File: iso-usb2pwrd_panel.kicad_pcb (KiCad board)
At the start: 2 copper layers, 75 x 74 mm, 204 parts, among them J1 USB_C_Receptacle_USB2.0_14P, J2 USB_C_Receptacle_USB2.0_14P, U1 ADuM3165, U2 R05C1TF05S, U3 TPS25820, Y1 24Mhz

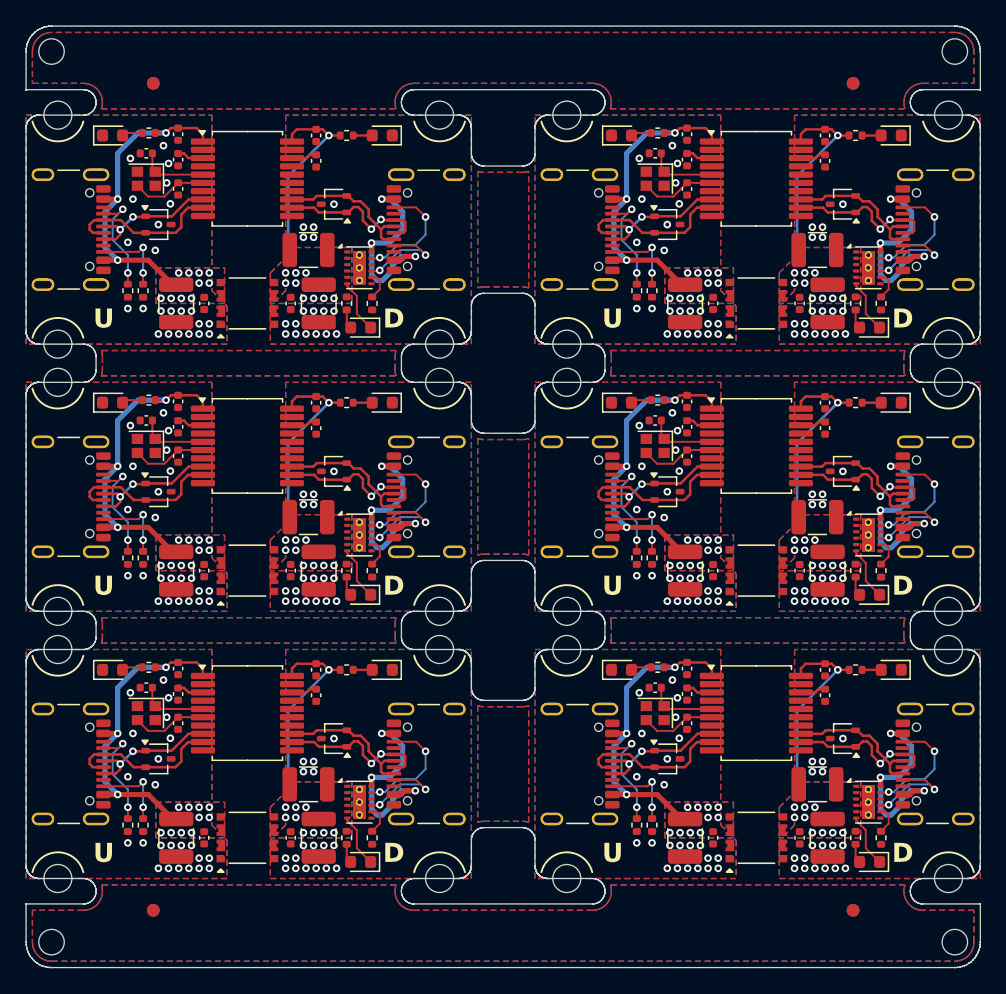
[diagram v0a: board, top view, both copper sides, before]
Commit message: update panel config: reduce vspace
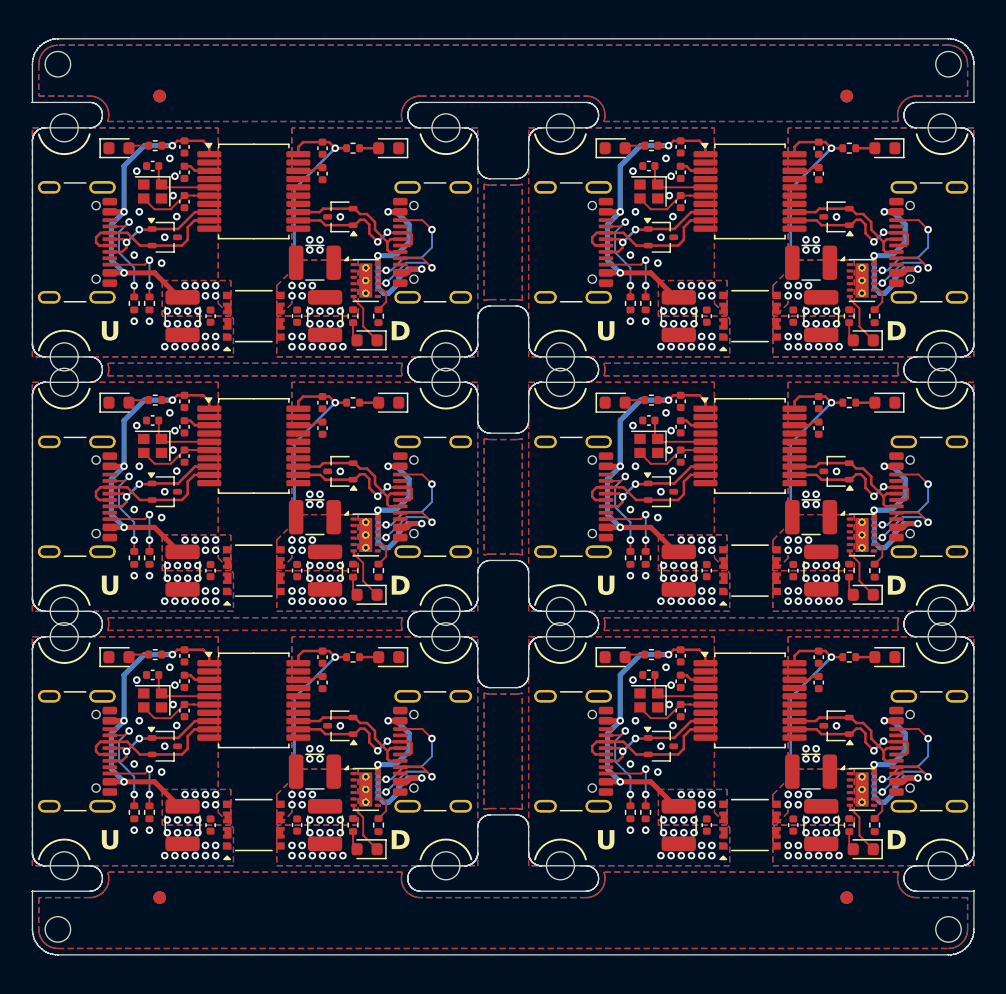
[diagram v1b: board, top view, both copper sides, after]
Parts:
- removed the C1 at (122.8, 84.8)
- removed the C1 at (122.8, 105.8)
- removed the C1 at (162.8, 126.8)
- removed the C1 at (162.8, 84.8)
- removed the C1 at (122.8, 126.8)
- removed the C1 at (162.8, 105.8)
- removed the C10 at (133.8, 71.6)
- removed the C10 at (173.8, 71.6)
- removed the C10 at (173.8, 92.6)
- removed the C10 at (133.8, 92.6)
- removed the C10 at (133.8, 113.6)
- removed the C10 at (173.8, 113.6)
- removed the C11 at (173.2, 122.6)
- removed the C11 at (133.2, 80.6)
- removed the C11 at (133.2, 122.6)
- removed the C11 at (173.2, 80.6)
- removed the C11 at (133.2, 101.6)
- removed the C11 at (173.2, 101.6)
- removed the C2 at (125.0, 84.8)
- removed the C2 at (125.0, 126.8)
- removed the C2 at (165.0, 84.8)
- removed the C2 at (125.0, 105.8)
- removed the C2 at (165.0, 126.8)
- removed the C2 at (165.0, 105.8)
- removed the C3 at (174.0, 84.8)
- removed the C3 at (134.0, 84.8)
- removed the C3 at (174.0, 105.8)
- removed the C3 at (174.0, 126.8)
- removed the C3 at (134.0, 126.8)
- removed the C3 at (134.0, 105.8)
- removed the C4 at (171.8, 84.8)
- removed the C4 at (131.8, 84.8)
- removed the C4 at (171.8, 105.8)
- removed the C4 at (171.8, 126.8)
- removed the C4 at (131.8, 126.8)
- removed the C4 at (131.8, 105.8)
- removed the C5 at (160.4, 94.0)
- removed the C5 at (160.4, 73.0)
- removed the C5 at (120.5, 94.0)
- removed the C5 at (120.5, 115.0)
- removed the C5 at (160.4, 115.0)
- removed the C5 at (120.5, 73.0)
- removed the C6 at (162.9, 75.8)
- removed the C6 at (162.9, 117.8)
- removed the C6 at (123.0, 117.8)
- removed the C6 at (123.0, 96.8)
- removed the C6 at (162.9, 96.8)
- removed the C6 at (123.0, 75.8)
- removed the C7 at (162.9, 94.5)
- removed the C7 at (123.0, 73.5)
- removed the C7 at (162.9, 115.5)
- removed the C7 at (123.0, 94.5)
- removed the C7 at (123.0, 115.5)
- removed the C7 at (162.9, 73.5)
- removed the C8 at (123.0, 92.5)
- removed the C8 at (162.9, 71.5)
- removed the C8 at (162.9, 113.5)
- removed the C8 at (162.9, 92.5)
- removed the C8 at (123.0, 71.5)
- removed the C8 at (123.0, 113.5)
- removed the C9 at (173.8, 73.6)
- removed the C9 at (173.8, 115.6)
- removed the C9 at (133.8, 73.6)
- removed the C9 at (133.8, 115.6)
- removed the C9 at (173.8, 94.6)
- removed the C9 at (133.8, 94.6)
- removed the D1 at (161.4, 78.6)
- removed the D1 at (161.4, 99.6)
- removed the D1 at (121.4, 78.6)
- removed the D1 at (121.4, 120.6)
- removed the D1 at (161.4, 120.6)
- removed the D1 at (121.4, 99.6)
- removed the D2 at (135.2, 119.0)
- removed the D2 at (135.2, 77.0)
- removed the D2 at (175.2, 98.0)
- removed the D2 at (175.2, 119.0)
- removed the D2 at (175.2, 77.0)
- removed the D2 at (135.2, 98.0)
- removed the D3 at (177.3, 128.7)
- removed the D3 at (137.3, 107.7)
- removed the D3 at (137.3, 128.7)
- removed the D3 at (177.3, 107.7)
- removed the D3 at (177.3, 86.7)
- removed the D3 at (137.3, 86.7)
- removed the D4 at (179.0, 92.6)
- removed the D4 at (139.0, 92.6)
- removed the D4 at (179.0, 113.6)
- removed the D4 at (139.0, 113.6)
- removed the D4 at (139.0, 71.6)
- removed the D4 at (179.0, 71.6)
- removed the D5 at (157.8, 113.6)
- removed the D5 at (157.8, 92.6)
- removed the D5 at (157.8, 71.6)
- removed the D5 at (117.8, 92.6)
- removed the D5 at (117.8, 113.6)
- removed the D5 at (117.8, 71.6)
- removed the H1 at (153.5, 109.0)
- removed the H1 at (153.5, 130.0)
- removed the H1 at (113.5, 88.0)
- removed the H1 at (153.5, 88.0)
- removed the H1 at (113.5, 109.0)
- removed the H1 at (113.5, 130.0)
- removed the H2 at (153.5, 91.0)
- removed the H2 at (113.5, 70.0)
- removed the H2 at (153.5, 112.0)
- removed the H2 at (113.5, 112.0)
- removed the H2 at (153.5, 70.0)
- removed the H2 at (113.5, 91.0)
- removed the H3 at (143.5, 112.0)
- removed the H3 at (183.5, 91.0)
- removed the H3 at (143.5, 70.0)
- removed the H3 at (183.5, 112.0)
- removed the H3 at (143.5, 91.0)
- removed the H3 at (183.5, 70.0)
- removed the H4 at (183.5, 88.0)
- removed the H4 at (143.5, 88.0)
- removed the H4 at (143.5, 109.0)
- removed the H4 at (183.5, 130.0)
- removed the H4 at (183.5, 109.0)
- removed the H4 at (143.5, 130.0)
- removed the J1 at (113.4, 79.0)
- removed the J1 at (113.4, 121.0)
- removed the J1 at (153.4, 121.0)
- removed the J1 at (113.4, 100.0)
- removed the J1 at (153.4, 100.0)
- removed the J1 at (153.4, 79.0)
- removed the J2 at (143.6, 121.0)
- removed the J2 at (183.6, 100.0)
- removed the J2 at (143.6, 79.0)
- removed the J2 at (143.6, 100.0)
- removed the J2 at (183.6, 121.0)
- removed the J2 at (183.6, 79.0)
- removed the R1 at (160.2, 83.8)
- removed the R1 at (120.2, 104.8)
- removed the R1 at (160.2, 104.8)
- removed the R1 at (120.2, 125.8)
- removed the R1 at (160.2, 125.8)
- removed the R1 at (120.2, 83.8)
- removed the R2 at (119.0, 104.8)
- removed the R2 at (159.0, 125.8)
- removed the R2 at (159.0, 104.8)
- removed the R2 at (119.0, 83.8)
- removed the R2 at (159.0, 83.8)
- removed the R2 at (119.0, 125.8)
- removed the R3 at (138.2, 126.8)
- removed the R3 at (178.2, 84.8)
- removed the R3 at (178.2, 126.8)
- removed the R3 at (138.2, 105.8)
- removed the R3 at (178.2, 105.8)
- removed the R3 at (138.2, 84.8)
- removed the R4 at (176.2, 84.8)
- removed the R4 at (136.2, 126.8)
- removed the R4 at (136.2, 84.8)
- removed the R4 at (176.2, 105.8)
- removed the R4 at (176.2, 126.8)
- removed the R4 at (136.2, 105.8)
- removed the R5 at (136.2, 113.6)
- removed the R5 at (136.2, 71.6)
- removed the R5 at (176.2, 113.6)
- removed the R5 at (176.2, 92.6)
- removed the R5 at (176.2, 71.6)
- removed the R5 at (136.2, 92.6)
- removed the R6 at (120.7, 113.4)
- removed the R6 at (160.7, 92.4)
- removed the R6 at (120.7, 71.4)
- removed the R6 at (160.7, 113.4)
- removed the R6 at (120.7, 92.4)
- removed the R6 at (160.7, 71.4)
- removed the U1 at (128.4, 75.0)
- removed the U1 at (128.4, 96.0)
- removed the U1 at (168.4, 96.0)
- removed the U1 at (168.4, 117.0)
- removed the U1 at (128.4, 117.0)
- removed the U1 at (168.4, 75.0)
- removed the U2 at (128.4, 84.8)
- removed the U2 at (128.4, 126.8)
- removed the U2 at (128.4, 105.8)
- removed the U2 at (168.4, 126.8)
- removed the U2 at (168.4, 84.8)
- removed the U2 at (168.4, 105.8)
- removed the U3 at (137.2, 82.0)
- removed the U3 at (137.2, 103.0)
- removed the U3 at (177.2, 103.0)
- removed the U3 at (137.2, 124.0)
- removed the U3 at (177.2, 82.0)
- removed the U3 at (177.2, 124.0)
- removed the Y1 at (160.4, 75.0)
- removed the Y1 at (160.4, 96.0)
- removed the Y1 at (120.5, 117.0)
- removed the Y1 at (120.5, 75.0)
- removed the Y1 at (120.5, 96.0)
- removed the Y1 at (160.4, 117.0)
- added C1: 22u, Capacitor_SMD:C_1210_3225Metric, F.Cu at (162.3, 85.8)
- added C1: 22u, Capacitor_SMD:C_1210_3225Metric, F.Cu at (162.3, 105.8)
- added C1: 22u, Capacitor_SMD:C_1210_3225Metric, F.Cu at (123.3, 105.8)
- added C1: 22u, Capacitor_SMD:C_1210_3225Metric, F.Cu at (123.3, 125.8)
- added C1: 22u, Capacitor_SMD:C_1210_3225Metric, F.Cu at (123.3, 85.8)
- added C1: 22u, Capacitor_SMD:C_1210_3225Metric, F.Cu at (162.3, 125.8)
- added C10: 0.1u, Capacitor_SMD:C_0402_1005Metric, F.Cu at (134.3, 112.6)
- added C10: 0.1u, Capacitor_SMD:C_0402_1005Metric, F.Cu at (173.3, 92.6)
- added C10: 0.1u, Capacitor_SMD:C_0402_1005Metric, F.Cu at (134.3, 92.6)
- added C10: 0.1u, Capacitor_SMD:C_0402_1005Metric, F.Cu at (173.3, 72.6)
- added C10: 0.1u, Capacitor_SMD:C_0402_1005Metric, F.Cu at (134.3, 72.6)
- added C10: 0.1u, Capacitor_SMD:C_0402_1005Metric, F.Cu at (173.3, 112.6)
- added C11: 22u, Capacitor_SMD:C_1210_3225Metric, F.Cu at (133.7, 81.6)
- added C11: 22u, Capacitor_SMD:C_1210_3225Metric, F.Cu at (172.7, 81.6)
- added C11: 22u, Capacitor_SMD:C_1210_3225Metric, F.Cu at (133.7, 121.6)
- added C11: 22u, Capacitor_SMD:C_1210_3225Metric, F.Cu at (172.7, 101.6)
- added C11: 22u, Capacitor_SMD:C_1210_3225Metric, F.Cu at (172.7, 121.6)
- added C11: 22u, Capacitor_SMD:C_1210_3225Metric, F.Cu at (133.7, 101.6)
- added C2: 0.1u, Capacitor_SMD:C_0402_1005Metric, F.Cu at (125.5, 105.8)
- added C2: 0.1u, Capacitor_SMD:C_0402_1005Metric, F.Cu at (164.5, 85.8)
- added C2: 0.1u, Capacitor_SMD:C_0402_1005Metric, F.Cu at (125.5, 85.8)
- added C2: 0.1u, Capacitor_SMD:C_0402_1005Metric, F.Cu at (164.5, 125.8)
- added C2: 0.1u, Capacitor_SMD:C_0402_1005Metric, F.Cu at (164.5, 105.8)
- added C2: 0.1u, Capacitor_SMD:C_0402_1005Metric, F.Cu at (125.5, 125.8)
- added C3: 22u, Capacitor_SMD:C_1210_3225Metric, F.Cu at (134.5, 125.8)
- added C3: 22u, Capacitor_SMD:C_1210_3225Metric, F.Cu at (173.5, 105.8)
- added C3: 22u, Capacitor_SMD:C_1210_3225Metric, F.Cu at (134.5, 85.8)
- added C3: 22u, Capacitor_SMD:C_1210_3225Metric, F.Cu at (134.5, 105.8)
- added C3: 22u, Capacitor_SMD:C_1210_3225Metric, F.Cu at (173.5, 125.8)
- added C3: 22u, Capacitor_SMD:C_1210_3225Metric, F.Cu at (173.5, 85.8)
- added C4: 0.1u, Capacitor_SMD:C_0402_1005Metric, F.Cu at (171.3, 105.8)
- added C4: 0.1u, Capacitor_SMD:C_0402_1005Metric, F.Cu at (132.3, 85.8)
- added C4: 0.1u, Capacitor_SMD:C_0402_1005Metric, F.Cu at (132.3, 125.8)
- added C4: 0.1u, Capacitor_SMD:C_0402_1005Metric, F.Cu at (171.3, 85.8)
- added C4: 0.1u, Capacitor_SMD:C_0402_1005Metric, F.Cu at (132.3, 105.8)
- added C4: 0.1u, Capacitor_SMD:C_0402_1005Metric, F.Cu at (171.3, 125.8)
- added C5: 15p, Capacitor_SMD:C_0402_1005Metric, F.Cu at (159.9, 94.0)
- added C5: 15p, Capacitor_SMD:C_0402_1005Metric, F.Cu at (159.9, 114.0)
- added C5: 15p, Capacitor_SMD:C_0402_1005Metric, F.Cu at (121.0, 114.0)
- added C5: 15p, Capacitor_SMD:C_0402_1005Metric, F.Cu at (121.0, 94.0)
- added C5: 15p, Capacitor_SMD:C_0402_1005Metric, F.Cu at (159.9, 74.0)
- added C5: 15p, Capacitor_SMD:C_0402_1005Metric, F.Cu at (121.0, 74.0)
- added C6: 15p, Capacitor_SMD:C_0402_1005Metric, F.Cu at (162.4, 96.8)
- added C6: 15p, Capacitor_SMD:C_0402_1005Metric, F.Cu at (123.5, 76.8)
- added C6: 15p, Capacitor_SMD:C_0402_1005Metric, F.Cu at (123.5, 96.8)
- added C6: 15p, Capacitor_SMD:C_0402_1005Metric, F.Cu at (123.5, 116.8)
- added C6: 15p, Capacitor_SMD:C_0402_1005Metric, F.Cu at (162.4, 76.8)
- added C6: 15p, Capacitor_SMD:C_0402_1005Metric, F.Cu at (162.4, 116.8)
- added C7: 0.1u, Capacitor_SMD:C_0402_1005Metric, F.Cu at (162.4, 114.5)
- added C7: 0.1u, Capacitor_SMD:C_0402_1005Metric, F.Cu at (162.4, 94.5)
- added C7: 0.1u, Capacitor_SMD:C_0402_1005Metric, F.Cu at (162.4, 74.5)
- added C7: 0.1u, Capacitor_SMD:C_0402_1005Metric, F.Cu at (123.5, 74.5)
- added C7: 0.1u, Capacitor_SMD:C_0402_1005Metric, F.Cu at (123.5, 94.5)
- added C7: 0.1u, Capacitor_SMD:C_0402_1005Metric, F.Cu at (123.5, 114.5)
- added C8: 0.1u, Capacitor_SMD:C_0402_1005Metric, F.Cu at (162.4, 92.5)
- added C8: 0.1u, Capacitor_SMD:C_0402_1005Metric, F.Cu at (123.5, 112.5)
- added C8: 0.1u, Capacitor_SMD:C_0402_1005Metric, F.Cu at (162.4, 112.5)
- added C8: 0.1u, Capacitor_SMD:C_0402_1005Metric, F.Cu at (123.5, 72.5)
- added C8: 0.1u, Capacitor_SMD:C_0402_1005Metric, F.Cu at (162.4, 72.5)
- added C8: 0.1u, Capacitor_SMD:C_0402_1005Metric, F.Cu at (123.5, 92.5)
- added C9: 0.1u, Capacitor_SMD:C_0402_1005Metric, F.Cu at (173.3, 114.6)
- added C9: 0.1u, Capacitor_SMD:C_0402_1005Metric, F.Cu at (173.3, 94.6)
- added C9: 0.1u, Capacitor_SMD:C_0402_1005Metric, F.Cu at (134.3, 74.6)
- added C9: 0.1u, Capacitor_SMD:C_0402_1005Metric, F.Cu at (134.3, 94.6)
- added C9: 0.1u, Capacitor_SMD:C_0402_1005Metric, F.Cu at (173.3, 74.6)
- added C9: 0.1u, Capacitor_SMD:C_0402_1005Metric, F.Cu at (134.3, 114.6)
- added D1: D_TVS_Dual_AAC, Package_TO_SOT_SMD:SOT-323_SC-70, F.Cu at (121.9, 79.6)
- added D1: D_TVS_Dual_AAC, Package_TO_SOT_SMD:SOT-323_SC-70, F.Cu at (160.9, 99.6)
- added D1: D_TVS_Dual_AAC, Package_TO_SOT_SMD:SOT-323_SC-70, F.Cu at (160.9, 119.6)
- added D1: D_TVS_Dual_AAC, Package_TO_SOT_SMD:SOT-323_SC-70, F.Cu at (121.9, 119.6)
- added D1: D_TVS_Dual_AAC, Package_TO_SOT_SMD:SOT-323_SC-70, F.Cu at (160.9, 79.6)
- added D1: D_TVS_Dual_AAC, Package_TO_SOT_SMD:SOT-323_SC-70, F.Cu at (121.9, 99.6)
- added D2: D_TVS_Dual_AAC, Package_TO_SOT_SMD:SOT-323_SC-70, F.Cu at (174.7, 118.0)
- added D2: D_TVS_Dual_AAC, Package_TO_SOT_SMD:SOT-323_SC-70, F.Cu at (174.7, 78.0)
- added D2: D_TVS_Dual_AAC, Package_TO_SOT_SMD:SOT-323_SC-70, F.Cu at (135.7, 78.0)
- added D2: D_TVS_Dual_AAC, Package_TO_SOT_SMD:SOT-323_SC-70, F.Cu at (174.7, 98.0)
- added D2: D_TVS_Dual_AAC, Package_TO_SOT_SMD:SOT-323_SC-70, F.Cu at (135.7, 118.0)
- added D2: D_TVS_Dual_AAC, Package_TO_SOT_SMD:SOT-323_SC-70, F.Cu at (135.7, 98.0)
- added D3: LED_Amber, LED_SMD:LED_0603_1608Metric, F.Cu at (137.8, 127.7)
- added D3: LED_Amber, LED_SMD:LED_0603_1608Metric, F.Cu at (176.8, 87.7)
- added D3: LED_Amber, LED_SMD:LED_0603_1608Metric, F.Cu at (176.8, 127.7)
- added D3: LED_Amber, LED_SMD:LED_0603_1608Metric, F.Cu at (137.8, 87.7)
- added D3: LED_Amber, LED_SMD:LED_0603_1608Metric, F.Cu at (176.8, 107.7)
- added D3: LED_Amber, LED_SMD:LED_0603_1608Metric, F.Cu at (137.8, 107.7)
- added D4: LED_Green, LED_SMD:LED_0603_1608Metric, F.Cu at (139.5, 92.6)
- added D4: LED_Green, LED_SMD:LED_0603_1608Metric, F.Cu at (178.5, 72.6)
- added D4: LED_Green, LED_SMD:LED_0603_1608Metric, F.Cu at (178.5, 92.6)
- added D4: LED_Green, LED_SMD:LED_0603_1608Metric, F.Cu at (178.5, 112.6)
- added D4: LED_Green, LED_SMD:LED_0603_1608Metric, F.Cu at (139.5, 72.6)
- added D4: LED_Green, LED_SMD:LED_0603_1608Metric, F.Cu at (139.5, 112.6)
- added D5: LED_Green, LED_SMD:LED_0603_1608Metric, F.Cu at (118.3, 72.6)
- added D5: LED_Green, LED_SMD:LED_0603_1608Metric, F.Cu at (118.3, 112.6)
- added D5: LED_Green, LED_SMD:LED_0603_1608Metric, F.Cu at (157.3, 112.6)
- added D5: LED_Green, LED_SMD:LED_0603_1608Metric, F.Cu at (157.3, 72.6)
- added D5: LED_Green, LED_SMD:LED_0603_1608Metric, F.Cu at (118.3, 92.6)
- added D5: LED_Green, LED_SMD:LED_0603_1608Metric, F.Cu at (157.3, 92.6)
- added H1: MountingHole, MountingHole:MountingHole_2.2mm_M2, F.Cu at (114.0, 109.0)
- added H1: MountingHole, MountingHole:MountingHole_2.2mm_M2, F.Cu at (153.0, 109.0)
- added H1: MountingHole, MountingHole:MountingHole_2.2mm_M2, F.Cu at (114.0, 129.0)
- added H1: MountingHole, MountingHole:MountingHole_2.2mm_M2, F.Cu at (153.0, 129.0)
- added H1: MountingHole, MountingHole:MountingHole_2.2mm_M2, F.Cu at (153.0, 89.0)
- added H1: MountingHole, MountingHole:MountingHole_2.2mm_M2, F.Cu at (114.0, 89.0)
- added H2: MountingHole, MountingHole:MountingHole_2.2mm_M2, F.Cu at (153.0, 111.0)
- added H2: MountingHole, MountingHole:MountingHole_2.2mm_M2, F.Cu at (114.0, 111.0)
- added H2: MountingHole, MountingHole:MountingHole_2.2mm_M2, F.Cu at (153.0, 71.0)
- added H2: MountingHole, MountingHole:MountingHole_2.2mm_M2, F.Cu at (114.0, 91.0)
- added H2: MountingHole, MountingHole:MountingHole_2.2mm_M2, F.Cu at (114.0, 71.0)
- added H2: MountingHole, MountingHole:MountingHole_2.2mm_M2, F.Cu at (153.0, 91.0)
- added H3: MountingHole, MountingHole:MountingHole_2.2mm_M2, F.Cu at (183.0, 71.0)
- added H3: MountingHole, MountingHole:MountingHole_2.2mm_M2, F.Cu at (144.0, 111.0)
- added H3: MountingHole, MountingHole:MountingHole_2.2mm_M2, F.Cu at (144.0, 91.0)
- added H3: MountingHole, MountingHole:MountingHole_2.2mm_M2, F.Cu at (183.0, 91.0)
- added H3: MountingHole, MountingHole:MountingHole_2.2mm_M2, F.Cu at (144.0, 71.0)
- added H3: MountingHole, MountingHole:MountingHole_2.2mm_M2, F.Cu at (183.0, 111.0)
- added H4: MountingHole, MountingHole:MountingHole_2.2mm_M2, F.Cu at (183.0, 109.0)
- added H4: MountingHole, MountingHole:MountingHole_2.2mm_M2, F.Cu at (144.0, 89.0)
- added H4: MountingHole, MountingHole:MountingHole_2.2mm_M2, F.Cu at (144.0, 109.0)
- added H4: MountingHole, MountingHole:MountingHole_2.2mm_M2, F.Cu at (183.0, 129.0)
- added H4: MountingHole, MountingHole:MountingHole_2.2mm_M2, F.Cu at (144.0, 129.0)
- added H4: MountingHole, MountingHole:MountingHole_2.2mm_M2, F.Cu at (183.0, 89.0)
- added J1: USB_C_Receptacle_USB2.0_14P, Connector_USB:USB_C_Receptacle_GCT_USB4105-xx-A_16P_TopMnt_Horizontal, F.Cu at (152.9, 120.0)
- added J1: USB_C_Receptacle_USB2.0_14P, Connector_USB:USB_C_Receptacle_GCT_USB4105-xx-A_16P_TopMnt_Horizontal, F.Cu at (113.9, 80.0)
- added J1: USB_C_Receptacle_USB2.0_14P, Connector_USB:USB_C_Receptacle_GCT_USB4105-xx-A_16P_TopMnt_Horizontal, F.Cu at (152.9, 80.0)
- added J1: USB_C_Receptacle_USB2.0_14P, Connector_USB:USB_C_Receptacle_GCT_USB4105-xx-A_16P_TopMnt_Horizontal, F.Cu at (113.9, 120.0)
- added J1: USB_C_Receptacle_USB2.0_14P, Connector_USB:USB_C_Receptacle_GCT_USB4105-xx-A_16P_TopMnt_Horizontal, F.Cu at (152.9, 100.0)
- added J1: USB_C_Receptacle_USB2.0_14P, Connector_USB:USB_C_Receptacle_GCT_USB4105-xx-A_16P_TopMnt_Horizontal, F.Cu at (113.9, 100.0)
- added J2: USB_C_Receptacle_USB2.0_14P, Connector_USB:USB_C_Receptacle_GCT_USB4105-xx-A_16P_TopMnt_Horizontal, F.Cu at (144.1, 100.0)
- added J2: USB_C_Receptacle_USB2.0_14P, Connector_USB:USB_C_Receptacle_GCT_USB4105-xx-A_16P_TopMnt_Horizontal, F.Cu at (144.1, 80.0)
- added J2: USB_C_Receptacle_USB2.0_14P, Connector_USB:USB_C_Receptacle_GCT_USB4105-xx-A_16P_TopMnt_Horizontal, F.Cu at (183.1, 120.0)
- added J2: USB_C_Receptacle_USB2.0_14P, Connector_USB:USB_C_Receptacle_GCT_USB4105-xx-A_16P_TopMnt_Horizontal, F.Cu at (144.1, 120.0)
- added J2: USB_C_Receptacle_USB2.0_14P, Connector_USB:USB_C_Receptacle_GCT_USB4105-xx-A_16P_TopMnt_Horizontal, F.Cu at (183.1, 80.0)
- added J2: USB_C_Receptacle_USB2.0_14P, Connector_USB:USB_C_Receptacle_GCT_USB4105-xx-A_16P_TopMnt_Horizontal, F.Cu at (183.1, 100.0)
- added R1: 5.1K, Resistor_SMD:R_0402_1005Metric, F.Cu at (159.7, 104.8)
- added R1: 5.1K, Resistor_SMD:R_0402_1005Metric, F.Cu at (120.7, 84.8)
- added R1: 5.1K, Resistor_SMD:R_0402_1005Metric, F.Cu at (120.7, 124.8)
- added R1: 5.1K, Resistor_SMD:R_0402_1005Metric, F.Cu at (159.7, 124.8)
- added R1: 5.1K, Resistor_SMD:R_0402_1005Metric, F.Cu at (159.7, 84.8)
- added R1: 5.1K, Resistor_SMD:R_0402_1005Metric, F.Cu at (120.7, 104.8)
- added R2: 5.1K, Resistor_SMD:R_0402_1005Metric, F.Cu at (158.5, 84.8)
- added R2: 5.1K, Resistor_SMD:R_0402_1005Metric, F.Cu at (119.5, 124.8)
- added R2: 5.1K, Resistor_SMD:R_0402_1005Metric, F.Cu at (119.5, 84.8)
- added R2: 5.1K, Resistor_SMD:R_0402_1005Metric, F.Cu at (158.5, 124.8)
- added R2: 5.1K, Resistor_SMD:R_0402_1005Metric, F.Cu at (158.5, 104.8)
- added R2: 5.1K, Resistor_SMD:R_0402_1005Metric, F.Cu at (119.5, 104.8)
- added R3: 100K, Resistor_SMD:R_0402_1005Metric, F.Cu at (138.7, 85.8)
- added R3: 100K, Resistor_SMD:R_0402_1005Metric, F.Cu at (138.7, 125.8)
- added R3: 100K, Resistor_SMD:R_0402_1005Metric, F.Cu at (177.7, 105.8)
- added R3: 100K, Resistor_SMD:R_0402_1005Metric, F.Cu at (177.7, 85.8)
- added R3: 100K, Resistor_SMD:R_0402_1005Metric, F.Cu at (138.7, 105.8)
- added R3: 100K, Resistor_SMD:R_0402_1005Metric, F.Cu at (177.7, 125.8)
- added R4: 5.1K, Resistor_SMD:R_0402_1005Metric, F.Cu at (175.7, 105.8)
- added R4: 5.1K, Resistor_SMD:R_0402_1005Metric, F.Cu at (136.7, 85.8)
- added R4: 5.1K, Resistor_SMD:R_0402_1005Metric, F.Cu at (136.7, 105.8)
- added R4: 5.1K, Resistor_SMD:R_0402_1005Metric, F.Cu at (136.7, 125.8)
- added R4: 5.1K, Resistor_SMD:R_0402_1005Metric, F.Cu at (175.7, 125.8)
- added R4: 5.1K, Resistor_SMD:R_0402_1005Metric, F.Cu at (175.7, 85.8)
- added R5: 5.1K, Resistor_SMD:R_0402_1005Metric, F.Cu at (136.7, 112.6)
- added R5: 5.1K, Resistor_SMD:R_0402_1005Metric, F.Cu at (175.7, 112.6)
- added R5: 5.1K, Resistor_SMD:R_0402_1005Metric, F.Cu at (136.7, 92.6)
- added R5: 5.1K, Resistor_SMD:R_0402_1005Metric, F.Cu at (175.7, 72.6)
- added R5: 5.1K, Resistor_SMD:R_0402_1005Metric, F.Cu at (136.7, 72.6)
- added R5: 5.1K, Resistor_SMD:R_0402_1005Metric, F.Cu at (175.7, 92.6)
- added R6: 5.1K, Resistor_SMD:R_0402_1005Metric, F.Cu at (121.2, 92.4)
- added R6: 5.1K, Resistor_SMD:R_0402_1005Metric, F.Cu at (160.2, 112.4)
- added R6: 5.1K, Resistor_SMD:R_0402_1005Metric, F.Cu at (160.2, 72.4)
- added R6: 5.1K, Resistor_SMD:R_0402_1005Metric, F.Cu at (160.2, 92.4)
- added R6: 5.1K, Resistor_SMD:R_0402_1005Metric, F.Cu at (121.2, 112.4)
- added R6: 5.1K, Resistor_SMD:R_0402_1005Metric, F.Cu at (121.2, 72.4)
- added U1: ADuM3165, Package_SO:SSOP-20_5.3x7.2mm_P0.65mm, F.Cu at (128.9, 96.0)
- added U1: ADuM3165, Package_SO:SSOP-20_5.3x7.2mm_P0.65mm, F.Cu at (167.9, 96.0)
- added U1: ADuM3165, Package_SO:SSOP-20_5.3x7.2mm_P0.65mm, F.Cu at (167.9, 76.0)
- added U1: ADuM3165, Package_SO:SSOP-20_5.3x7.2mm_P0.65mm, F.Cu at (167.9, 116.0)
- added U1: ADuM3165, Package_SO:SSOP-20_5.3x7.2mm_P0.65mm, F.Cu at (128.9, 76.0)
- added U1: ADuM3165, Package_SO:SSOP-20_5.3x7.2mm_P0.65mm, F.Cu at (128.9, 116.0)
- added U2: R05C1TF05S, q-lab:Package_LGA-12_5x4mm, F.Cu at (128.9, 105.8)
- added U2: R05C1TF05S, q-lab:Package_LGA-12_5x4mm, F.Cu at (128.9, 85.8)
- added U2: R05C1TF05S, q-lab:Package_LGA-12_5x4mm, F.Cu at (167.9, 85.8)
- added U2: R05C1TF05S, q-lab:Package_LGA-12_5x4mm, F.Cu at (128.9, 125.8)
- added U2: R05C1TF05S, q-lab:Package_LGA-12_5x4mm, F.Cu at (167.9, 105.8)
- added U2: R05C1TF05S, q-lab:Package_LGA-12_5x4mm, F.Cu at (167.9, 125.8)
- added U3: TPS25820, Package_SON:WSON-12-1EP_3x2mm_P0.5mm_EP1x2.65_ThermalVias, F.Cu at (176.7, 83.0)
- added U3: TPS25820, Package_SON:WSON-12-1EP_3x2mm_P0.5mm_EP1x2.65_ThermalVias, F.Cu at (176.7, 123.0)
- added U3: TPS25820, Package_SON:WSON-12-1EP_3x2mm_P0.5mm_EP1x2.65_ThermalVias, F.Cu at (137.7, 103.0)
- added U3: TPS25820, Package_SON:WSON-12-1EP_3x2mm_P0.5mm_EP1x2.65_ThermalVias, F.Cu at (137.7, 123.0)
- added U3: TPS25820, Package_SON:WSON-12-1EP_3x2mm_P0.5mm_EP1x2.65_ThermalVias, F.Cu at (176.7, 103.0)
- added U3: TPS25820, Package_SON:WSON-12-1EP_3x2mm_P0.5mm_EP1x2.65_ThermalVias, F.Cu at (137.7, 83.0)
- added Y1: 24Mhz, Crystal:Crystal_SMD_2016-4Pin_2.0x1.6mm, F.Cu at (159.9, 96.0)
- added Y1: 24Mhz, Crystal:Crystal_SMD_2016-4Pin_2.0x1.6mm, F.Cu at (159.9, 76.0)
- added Y1: 24Mhz, Crystal:Crystal_SMD_2016-4Pin_2.0x1.6mm, F.Cu at (121.0, 96.0)
- added Y1: 24Mhz, Crystal:Crystal_SMD_2016-4Pin_2.0x1.6mm, F.Cu at (121.0, 76.0)
- added Y1: 24Mhz, Crystal:Crystal_SMD_2016-4Pin_2.0x1.6mm, F.Cu at (121.0, 116.0)
- added Y1: 24Mhz, Crystal:Crystal_SMD_2016-4Pin_2.0x1.6mm, F.Cu at (159.9, 116.0)
- moved KiKit_FID_B_1 1.12 mm to (121.5, 68.5)
- moved KiKit_FID_B_2 1.12 mm to (175.5, 68.5)
- moved KiKit_FID_B_3 1.12 mm to (121.5, 131.5)
- moved KiKit_FID_B_4 1.12 mm to (175.5, 131.5)
- moved KiKit_FID_T_1 1.12 mm to (121.5, 68.5)
- moved KiKit_FID_T_2 1.12 mm to (175.5, 68.5)
- moved KiKit_FID_T_3 1.12 mm to (121.5, 131.5)
- moved KiKit_FID_T_4 1.12 mm to (175.5, 131.5)
- moved KiKit_TO_1 1.12 mm to (113.5, 66.0)
- moved KiKit_TO_2 1.12 mm to (183.5, 66.0)
- moved KiKit_TO_3 1.12 mm to (113.5, 134.0)
- moved KiKit_TO_4 1.12 mm to (183.5, 134.0)
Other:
- board size 75 x 74 mm -> 74 x 72 mm

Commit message: add board rev
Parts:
- D1 (x6), D2 (x6): value D_TVS_Dual_AAC -> ESD752
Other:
- board text added: "R1.0.0"
